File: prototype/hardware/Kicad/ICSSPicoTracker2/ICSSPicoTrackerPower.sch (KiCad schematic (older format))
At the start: 0 parts

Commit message: Updated Scehematics and Footprints
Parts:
- added C81, C83, C84: https://www.murata.com/en-eu/products/productdata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, Capacitor_SMD:C_0603_1608Metric, symbol Device:C
- added C82, C85: 100nF, Capacitor_SMD:C_0603_1608Metric, symbol Device:C
- added J3: Conn_01x02, Connector_PinHeader_1.00mm:PinHeader_1x02_P1.00mm_Vertical, symbol Connector_Generic:Conn_01x02
- added L23: 2.2uH, Inductor_SMD:L_Taiyo-Yuden_NR-30xx, symbol Device:L
- added Q1: Q_PMOS_DGS, Package_TO_SOT_SMD:SOT-23, symbol Device:Q_PMOS_DGS
- added R10: 180K, Resistor_SMD:R_0603_1608Metric, symbol Device:R
- added R11: 10K, Resistor_SMD:R_0603_1608Metric, symbol Device:R
- added R7, R8: 100K, Resistor_SMD:R_0603_1608Metric, symbol Device:R
- added R9: 470K, Resistor_SMD:R_0603_1608Metric, symbol Device:R
- added U9: TPS61200DRC, Package_SON:Texas_S-PVSON-N10_ThermalVias, symbol Regulator_Switching:TPS61200DRC
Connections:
- new net: C82.1, U9.1 (VAUX)
- new net: R10.1, R9.2, U9.10 (FB)
- new net: L23.2, U9.3 (L)
- new net: Q1.1 (D), R7.1
- new net: C85.2, Q1.2 (G), R11.2
- new net +1V8: C83.1, C84.1, R9.1, U9.2 (VOUT)
- new net GND: C81.2, C82.2, C83.2, C84.2, J3.2 (Pin_2), R10.2, R8.2, U9.11 (PAD), U9.4 (PGND), U9.9 (GND)
- new net PWR_BVOLTS: R7.2, R8.1
- new net PWR_MEASURE: C85.1
- new net VMEM: C81.1, J3.1 (Pin_1), L23.1, Q1.3 (S), R11.1, U9.5 (VIN), U9.6 (EN), U9.7 (UVLO), U9.8 (PS)

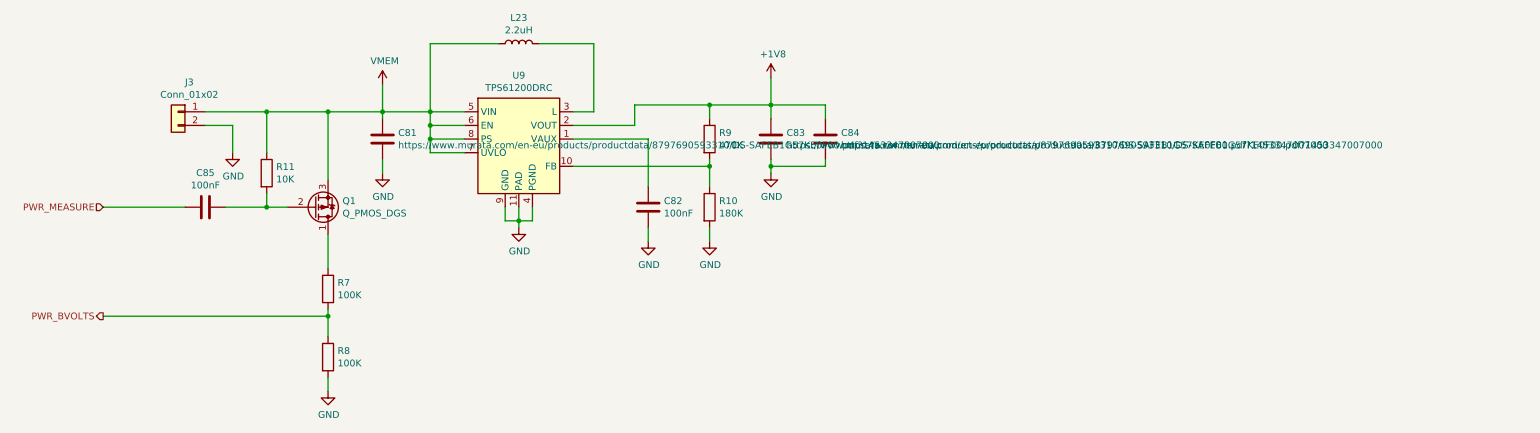
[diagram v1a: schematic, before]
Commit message: Add Antenna footprints
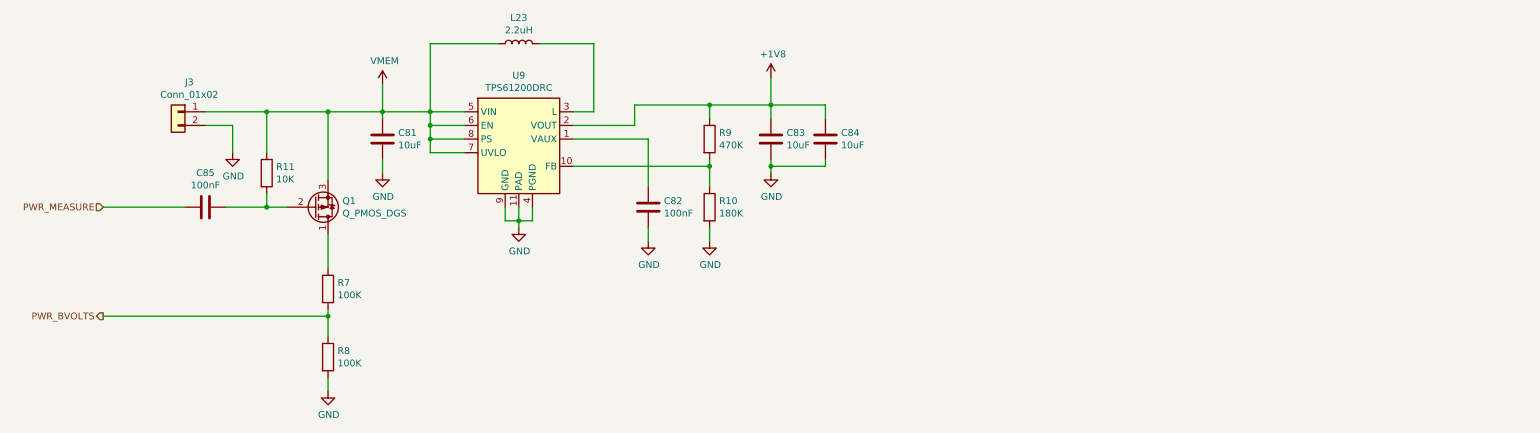
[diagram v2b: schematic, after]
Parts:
- C81, C83, C84: value https://www.murata.com/en-eu/products/productdata/8797690593310/DS-SAFEB1G57KE0F00.pdf?1453347007000 -> 10uF
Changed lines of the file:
@@
 P 4400 3350
 F 0 "C81" H 4515 3396 50  0000 L CNN
-F 1 "https://www.murata.com/en-eu/products/productdata/8797690593310/DS-SAFEB1G57KE0F00.pdf?1453347007000" H 4515 3305 50  0000 L CNN
+F 1 "10uF" H 4515 3305 50  0000 L CNN
 F 2 "Capacitor_SMD:C_0603_1608Metric" H 4438 3200 50  0001 C CNN
 F 3 "~" H 4400 3350 50  0001 C CNN
@@
 P 7250 3350
 F 0 "C83" H 7365 3396 50  0000 L CNN
-F 1 "https://www.murata.com/en-eu/products/productdata/8797690593310/DS-SAFEB1G57KE0F00.pdf?1453347007000" H 7365 3305 50  0000 L CNN
+F 1 "10uF" H 7365 3305 50  0000 L CNN
 F 2 "Capacitor_SMD:C_0603_1608Metric" H 7288 3200 50  0001 C CNN
 F 3 "~" H 7250 3350 50  0001 C CNN
@@
 P 7650 3350
 F 0 "C84" H 7765 3396 50  0000 L CNN
-F 1 "https://www.murata.com/en-eu/products/productdata/8797690593310/DS-SAFEB1G57KE0F00.pdf?1453347007000" H 7765 3305 50  0000 L CNN
+F 1 "10uF" H 7765 3305 50  0000 L CNN
 F 2 "Capacitor_SMD:C_0603_1608Metric" H 7688 3200 50  0001 C CNN
 F 3 "~" H 7650 3350 50  0001 C CNN

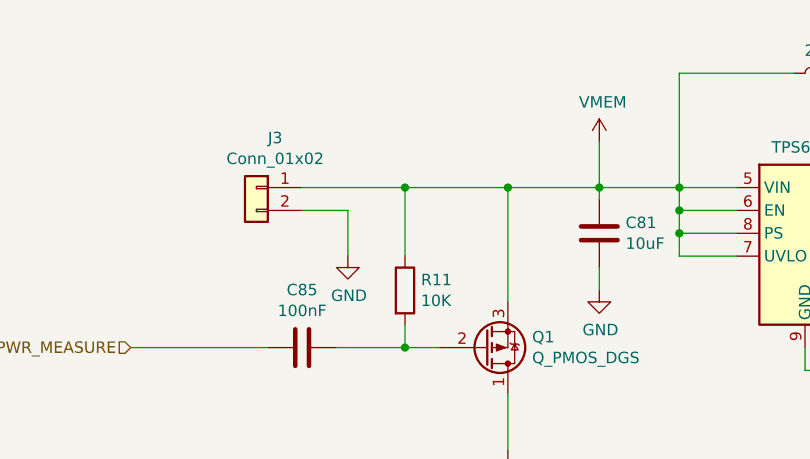
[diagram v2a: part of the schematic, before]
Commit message: Some more ERC fixes
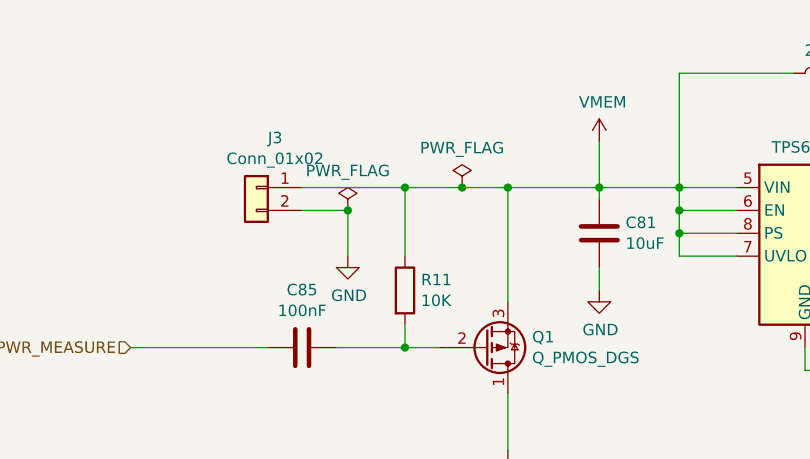
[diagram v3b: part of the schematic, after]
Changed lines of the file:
@@
 	6250 3250 6250 3100
-Wire Wire Line
-	6250 3100 6800 3100
 Wire Wire Line
 	7250 3100 7250 2900
@@
 Connection ~ 3550 3150
 Wire Wire Line
-	3550 3150 4000 3150
+	3550 3150 3800 3150
 Wire Wire Line
 	4000 3650 4000 3150
@@
 Wire Wire Line
 	2350 3850 2950 3850
+$Comp
+L power:PWR_FLAG #FLG0103
+U 1 1 5D62C890
+P 3800 3150
+F 0 "#FLG0103" H 3800 3225 50  0001 C CNN
+F 1 "PWR_FLAG" H 3800 3323 50  0000 C CNN
+F 2 "" H 3800 3150 50  0001 C CNN
+F 3 "~" H 3800 3150 50  0001 C CNN
+	1    3800 3150
+	1    0    0    -1
+$EndComp
+Connection ~ 3800 3150
+Wire Wire Line
+	3800 3150 4000 3150
+$Comp
+L power:PWR_FLAG #FLG0104
+U 1 1 5D62CCB0
+P 3300 3250
+F 0 "#FLG0104" H 3300 3325 50  0001 C CNN
+F 1 "PWR_FLAG" H 3300 3423 50  0000 C CNN
+F 2 "" H 3300 3250 50  0001 C CNN
+F 3 "~" H 3300 3250 50  0001 C CNN
+	1    3300 3250
+	1    0    0    -1
+$EndComp
+Connection ~ 3300 3250
+Wire Wire Line
+	6250 3100 6800 3100
 $EndSCHEMATC
